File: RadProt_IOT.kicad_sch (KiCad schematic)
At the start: 10 parts, among them J1 Conn_01x04_Pin, J2 Conn_01x04_Pin, J3 Conn_01x04_Pin, J4 OUT+, J5 OUT-, J6 Conn_02x05_Top_Bottom, SW1 Config, U1 RaspberryPi_Pico_W

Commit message: gcode generated...
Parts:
- renumbered J6 to J1, J1 to UART1, J2 to UART2, J3 to UART3
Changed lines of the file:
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@@
 		(dnp no)
 		(fields_autoplaced yes)
-		(property "Reference" "J2"
-			(at 71.755 99.06 0)
+		(property "Reference" "UART2"
+			(at 71.755 101.6 0)
 			(effects
 				(font
@@
 			(project ""
 				(path "/cff4cc2a-e2ab-4a74-8ae5-5e001e0fb180"
-					(reference "J2")
+					(reference "UART2")
 					(unit 1)
 				)
@@
 		(on_board no)
 		(dnp no)
-		(property "Reference" "J3"
+		(property "Reference" "UART3"
 			(at 71.755 142.24 0)
 			(effects
@@
 			(project ""
 				(path "/cff4cc2a-e2ab-4a74-8ae5-5e001e0fb180"
-					(reference "J3")
+					(reference "UART3")
 					(unit 1)
 				)
@@
 		(dnp no)
 		(fields_autoplaced yes)
-		(property "Reference" "J1"
-			(at 71.755 55.88 0)
+		(property "Reference" "UART1"
+			(at 71.755 58.42 0)
 			(effects
 				(font
@@
 			(project ""
 				(path "/cff4cc2a-e2ab-4a74-8ae5-5e001e0fb180"
-					(reference "J1")
+					(reference "UART1")
 					(unit 1)
 				)
@@
 		(dnp no)
 		(fields_autoplaced yes)
-		(property "Reference" "J6"
+		(property "Reference" "J1"
 			(at 215.9 97.79 0)
 			(effects
@@
 			(project ""
 				(path "/cff4cc2a-e2ab-4a74-8ae5-5e001e0fb180"
-					(reference "J6")
-					(unit 1)
-				)
+					(reference "J1")
+					(unit 1)
+				)

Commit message: prepared univprepared universal board with this layout
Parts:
- removed UART1, UART2, UART3: Conn_01x04_Pin, Connector_PinHeader_2.54mm:PinHeader_1x04_P2.54mm_Vertical, symbol Connector:Conn_01x04_Pin
- added UART0, UART2, UART3: Conn_01x04_Socket, Connector_PinSocket_2.54mm:PinSocket_1x04_P2.54mm_Vertical, symbol Connector:Conn_01x04_Socket
- R1: footprint Resistor_THT:R_Axial_DIN0204_L3.6mm_D1.6mm_P5.08mm_Horizontal -> Resistor_THT:R_Axial_DIN0204_L3.6mm_D1.6mm_P7.62mm_Horizontal
- renumbered J4 to J5, J5 to J6
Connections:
- net +5V: now also UART0.1 (Pin_1), UART2.1 (Pin_1), UART3.1 (Pin_1)
- net GND: now also R1.2, UART0.4 (Pin_4), UART2.4 (Pin_4), UART3.4 (Pin_4); no longer D1.1 (K)
- net UART0_RX: now also UART0.2 (Pin_2)
- net UART2_RX: now also UART2.2 (Pin_2)
- net UART3_RX: now also UART3.2 (Pin_2)
- net at U1.12 (GPIO9): now also D1.2 (A)
- net at U1.19 (GPIO14): no longer SW1.2
- net at U1.20 (GPIO15): now also SW1.2; no longer R1.1
- new net: D1.1 (K), R1.1
- no-connect marks 24 -> 23
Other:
- moved on the sheet: D1, R1, SW1

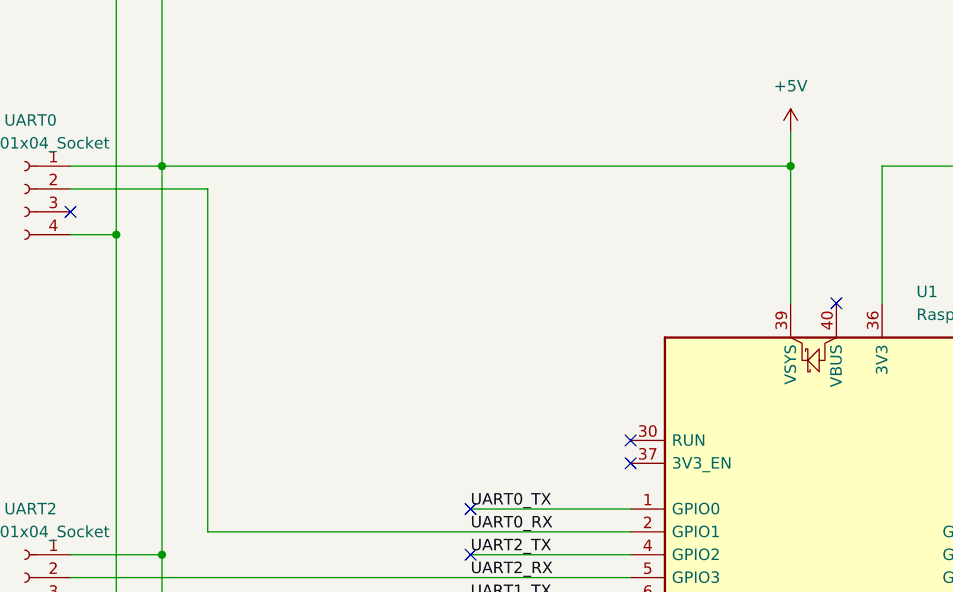
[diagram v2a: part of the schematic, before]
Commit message: added Power Ledd
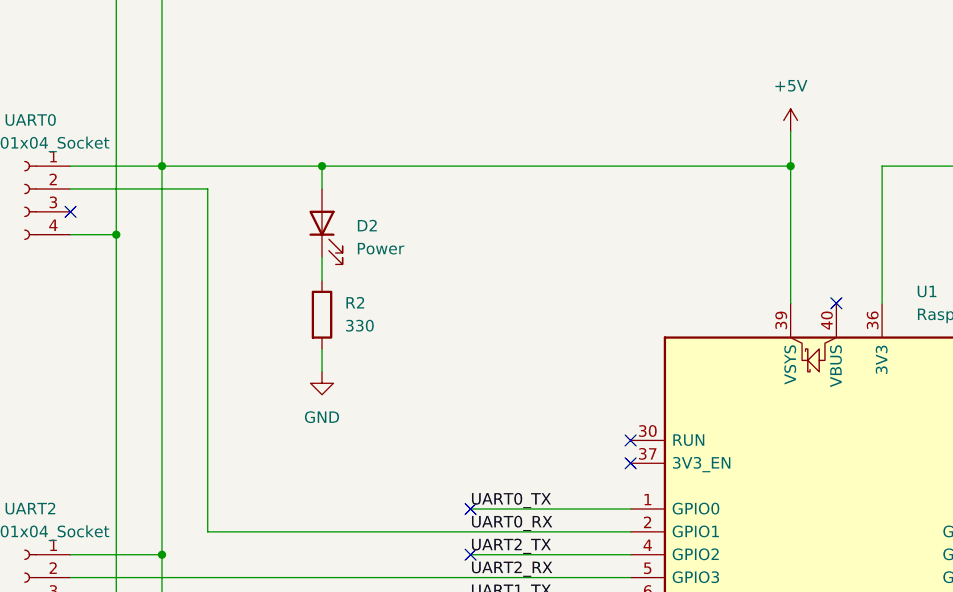
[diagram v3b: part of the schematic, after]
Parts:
- added D2: Power, LED_THT:LED_D3.0mm, symbol Device:LED
- added R2: 330, Resistor_THT:R_Axial_DIN0204_L3.6mm_D1.6mm_P7.62mm_Horizontal, symbol Device:R
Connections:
- net +5V: now also D2.2 (A)
- net GND: now also R2.2
- new net: D2.1 (K), R2.1

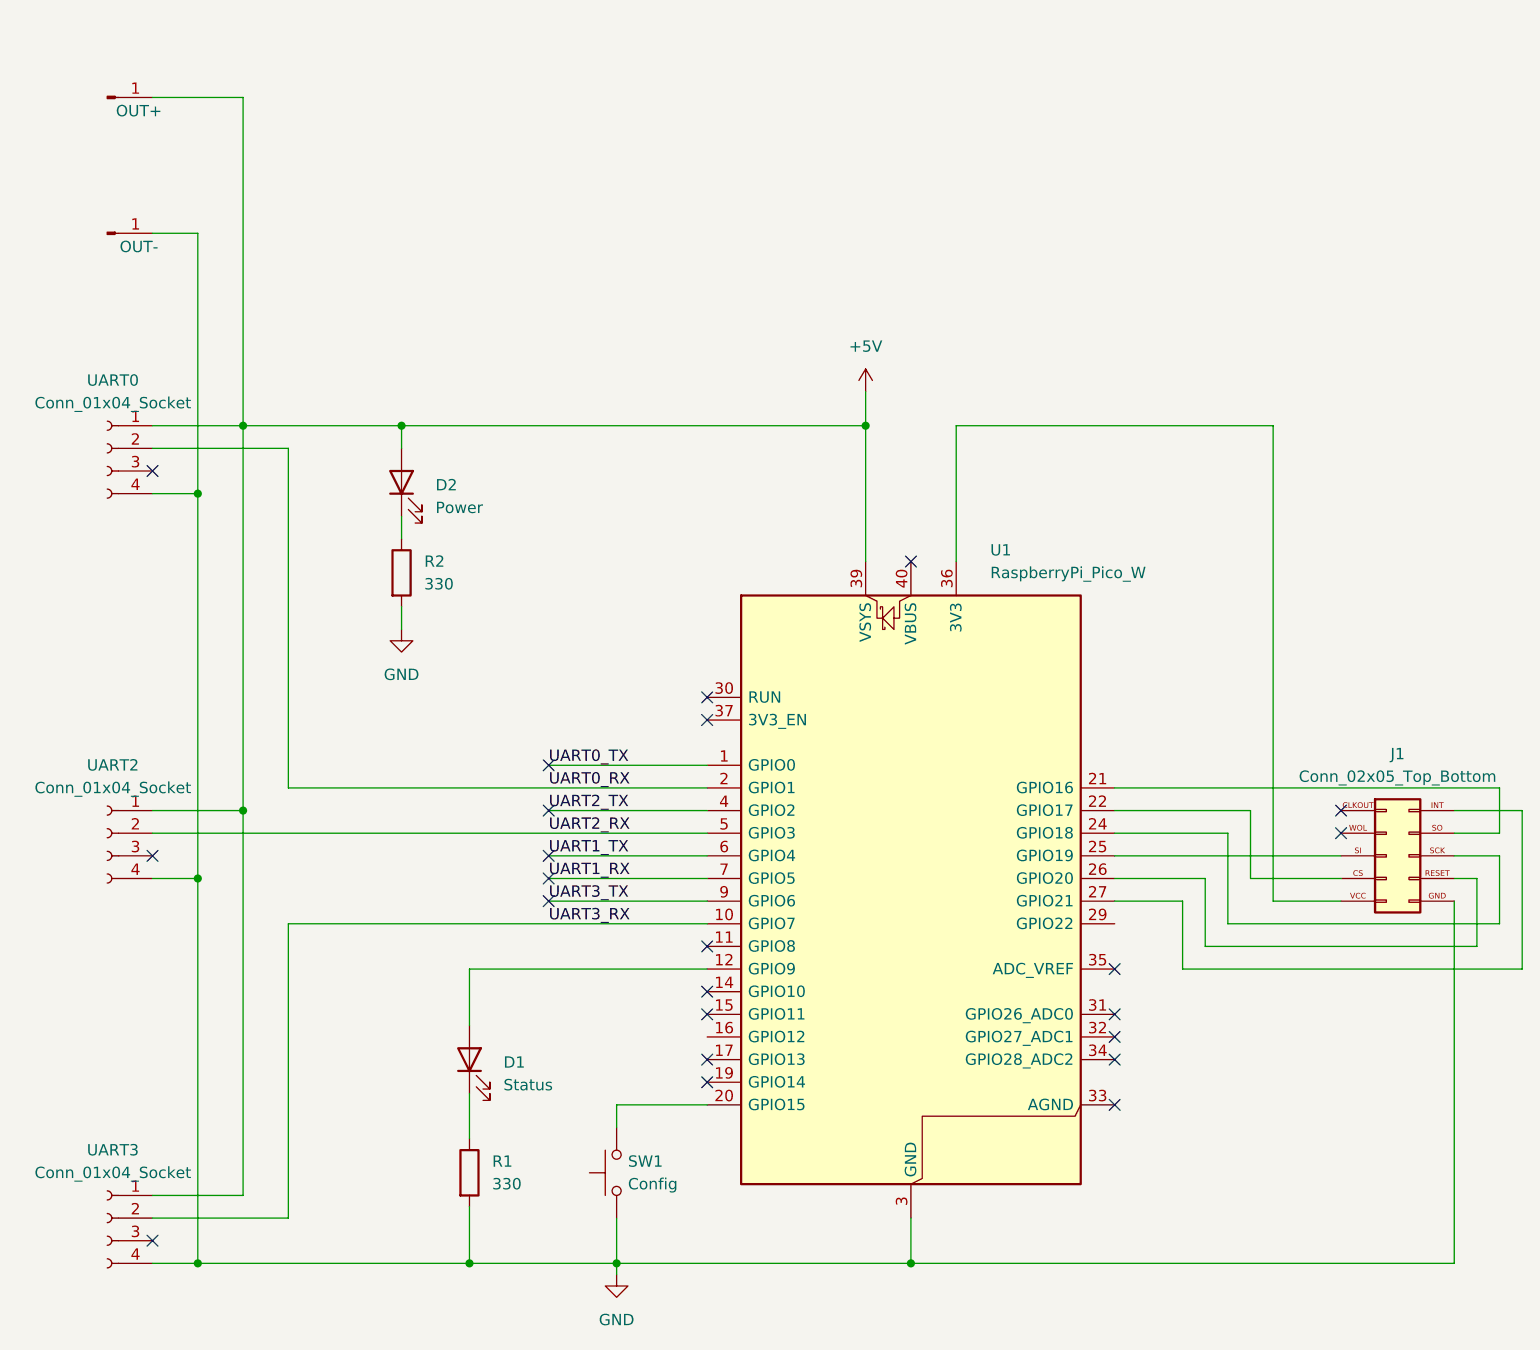
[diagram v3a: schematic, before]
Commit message: powering max3232's from 3V3 (RPi Pico's internal SMPS)
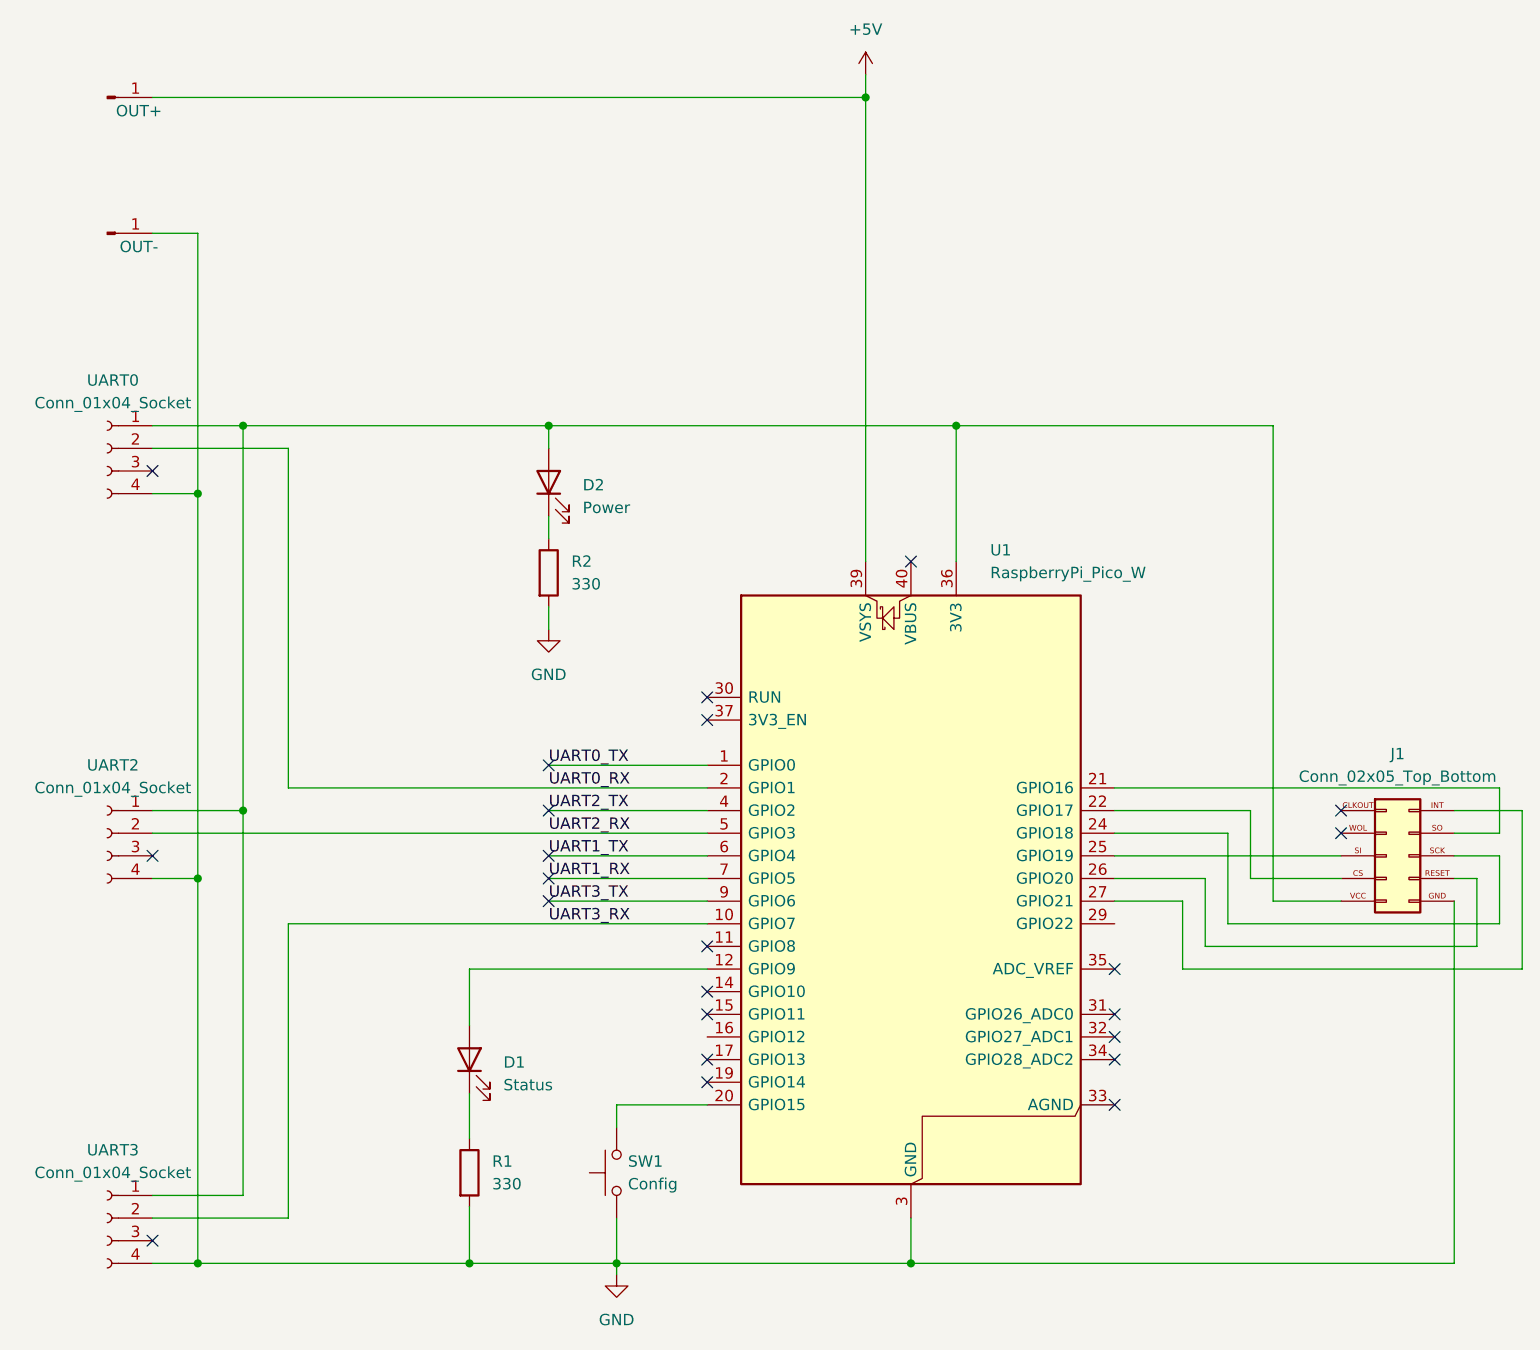
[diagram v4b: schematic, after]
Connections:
- net +5V: no longer D2.2 (A), UART0.1 (Pin_1), UART2.1 (Pin_1), UART3.1 (Pin_1)
- net at J1.VCC, U1.36 (3V3): now also D2.2 (A), UART0.1 (Pin_1), UART2.1 (Pin_1), UART3.1 (Pin_1)
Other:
- moved on the sheet: D2, R2
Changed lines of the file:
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@@
 	(paper "A4")
 	(junction
-		(at 111.76 154.94)
+		(at 166.37 60.96)
 		(diameter 0)
 		(color 0 0 0 0)
 	)
 	(junction
-		(at 156.21 60.96)
+		(at 111.76 154.94)
 		(diameter 0)
 		(color 0 0 0 0)
@@
 	)
 	(junction
-		(at 104.14 60.96)
+		(at 120.65 60.96)
 		(diameter 0)
 		(color 0 0 0 0)
 	)
 	(junction
-		(at 86.36 60.96)
+		(at 156.21 24.13)
 		(diameter 0)
 		(color 0 0 0 0)
@@
 	)
 	(junction
+		(at 86.36 60.96)
+		(diameter 0)
+		(color 0 0 0 0)
+	)
+	(junction
 		(at 81.28 154.94)
 		(diameter 0)
@@
 	(wire
 		(pts
-			(xy 104.14 60.96) (xy 104.14 63.5)
+			(xy 120.65 60.96) (xy 120.65 63.5)
 		)
 		(stroke
@@
 	(wire
 		(pts
-			(xy 104.14 71.12) (xy 104.14 73.66)
+			(xy 120.65 71.12) (xy 120.65 73.66)
 		)
 		(stroke
@@
 	(wire
 		(pts
-			(xy 156.21 60.96) (xy 156.21 76.2)
-		)
-		(stroke
-			(width 0)
-			(type default)
-		)
-	)
-	(wire
-		(pts
 			(xy 120.65 114.3) (xy 138.43 114.3)
 		)
@@
 	(wire
 		(pts
+			(xy 120.65 60.96) (xy 166.37 60.96)
+		)
+		(stroke
+			(width 0)
+			(type default)
+		)
+	)
+	(wire
+		(pts
 			(xy 184.15 104.14) (xy 199.39 104.14)
 		)
@@
 	(wire
 		(pts
+			(xy 76.2 24.13) (xy 156.21 24.13)
+		)
+		(stroke
+			(width 0)
+			(type default)
+		)
+	)
+	(wire
+		(pts
 			(xy 81.28 39.37) (xy 81.28 68.58)
 		)
@@
 	(wire
 		(pts
-			(xy 104.14 60.96) (xy 156.21 60.96)
-		)
-		(stroke
-			(width 0)
-			(type default)
-		)
-	)
-	(wire
-		(pts
 			(xy 184.15 111.76) (xy 194.31 111.76)
 		)
@@
 	(wire
 		(pts
-			(xy 104.14 81.28) (xy 104.14 83.82)
+			(xy 120.65 81.28) (xy 120.65 83.82)
 		)
 		(stroke
@@
 	(wire
 		(pts
-			(xy 76.2 24.13) (xy 86.36 24.13)
-		)
-		(stroke
-			(width 0)
-			(type default)
-		)
-	)
-	(wire
-		(pts
-			(xy 86.36 60.96) (xy 104.14 60.96)
+			(xy 201.93 60.96) (xy 166.37 60.96)
 		)
 		(stroke
@@
 	(wire
 		(pts
-			(xy 201.93 60.96) (xy 166.37 60.96)
+			(xy 76.2 106.68) (xy 138.43 106.68)
 		)
 		(stroke
@@
 	(wire
 		(pts
-			(xy 76.2 106.68) (xy 138.43 106.68)
+			(xy 128.27 154.94) (xy 161.29 154.94)
 		)
 		(stroke
@@
 	(wire
 		(pts
-			(xy 128.27 154.94) (xy 161.29 154.94)
+			(xy 156.21 24.13) (xy 156.21 76.2)
 		)
 		(stroke
@@
 	(wire
 		(pts
-			(xy 156.21 57.15) (xy 156.21 60.96)
+			(xy 194.31 111.76) (xy 194.31 119.38)
 		)
 		(stroke
@@
 	(wire
 		(pts
-			(xy 194.31 111.76) (xy 194.31 119.38)
+			(xy 76.2 104.14) (xy 86.36 104.14)
 		)
 		(stroke
@@
 	(wire
 		(pts
-			(xy 76.2 104.14) (xy 86.36 104.14)
+			(xy 156.21 24.13) (xy 156.21 21.59)
 		)
 		(stroke
@@
 	(wire
 		(pts
-			(xy 86.36 60.96) (xy 86.36 24.13)
+			(xy 86.36 60.96) (xy 120.65 60.96)
 		)
 		(stroke
@@
 	(symbol
 		(lib_id "Device:R")
-		(at 104.14 77.47 0)
+		(at 120.65 77.47 0)
 		(unit 1)
 		(exclude_from_sim no)
@@
 		(fields_autoplaced yes)
 		(property "Reference" "R2"
-			(at 106.68 76.1999 0)
+			(at 123.19 76.1999 0)
 			(effects
 				(font
@@
 		)
 		(property "Value" "330"
-			(at 106.68 78.7399 0)
+			(at 123.19 78.7399 0)
 			(effects
 				(font
@@
 		)
 		(property "Footprint" "Resistor_THT:R_Axial_DIN0204_L3.6mm_D1.6mm_P7.62mm_Horizontal"
-			(at 102.362 77.47 90)
+			(at 118.872 77.47 90)
 			(effects
 				(font
@@
 		)
 		(property "Datasheet" "~"
-			(at 104.14 77.47 0)
+			(at 120.65 77.47 0)
 			(effects
 				(font
@@
 		)
 		(property "Description" "Resistor"
-			(at 104.14 77.47 0)
+			(at 120.65 77.47 0)
 			(effects
 				(font
@@
 	(symbol
 		(lib_id "Device:LED")
-		(at 104.14 67.31 90)
+		(at 120.65 67.31 90)
 		(unit 1)
 		(exclude_from_sim no)
@@
 		(fields_autoplaced yes)
 		(property "Reference" "D2"
-			(at 107.95 67.6274 90)
+			(at 124.46 67.6274 90)
 			(effects
 				(font
@@
 		)
 		(property "Value" "Power"
-			(at 107.95 70.1674 90)
+			(at 124.46 70.1674 90)
 			(effects
 				(font
@@
 		)
 		(property "Footprint" "LED_THT:LED_D3.0mm"
-			(at 104.14 67.31 0)
+			(at 120.65 67.31 0)
 			(effects
 				(font
@@
 		)
 		(property "Datasheet" "~"
-			(at 104.14 67.31 0)
+			(at 120.65 67.31 0)
 			(effects
 				(font
@@
 		)
 		(property "Description" "Light emitting diode"
-			(at 104.14 67.31 0)
+			(at 120.65 67.31 0)
 			(effects
 				(font
@@
 		)
 		(property "Sim.Pins" "1=K 2=A"
-			(at 104.14 67.31 0)
+			(at 120.65 67.31 0)
 			(effects
 				(font
@@
 	(symbol
 		(lib_id "power:+5V")
-		(at 156.21 57.15 0)
+		(at 156.21 21.59 0)
 		(unit 1)
 		(exclude_from_sim no)
@@
 		(fields_autoplaced yes)
 		(property "Reference" "#PWR02"
-			(at 156.21 60.96 0)
+			(at 156.21 25.4 0)
 			(effects
 				(font
@@
 		)
 		(property "Value" "+5V"
-			(at 156.21 52.07 0)
+			(at 156.21 16.51 0)
 			(effects
 				(font
@@
 		)
 		(property "Footprint" ""
-			(at 156.21 57.15 0)
+			(at 156.21 21.59 0)
 			(effects
 				(font
@@
 		)
 		(property "Datasheet" ""
-			(at 156.21 57.15 0)
+			(at 156.21 21.59 0)
 			(effects
 				(font
@@
 		)
 		(property "Description" "Power symbol creates a global label with name \"+5V\""
-			(at 156.21 57.15 0)
+			(at 156.21 21.59 0)
 			(effects
 				(font
@@
 	(symbol
 		(lib_id "power:GND")
-		(at 104.14 83.82 0)
+		(at 120.65 83.82 0)
 		(unit 1)
 		(exclude_from_sim no)
@@
 		(fields_autoplaced yes)
 		(property "Reference" "#PWR03"
-			(at 104.14 90.17 0)
+			(at 120.65 90.17 0)
 			(effects
 				(font
@@
 		)
 		(property "Value" "GND"
-			(at 104.14 88.9 0)
+			(at 120.65 88.9 0)
 			(effects
 				(font
@@
 		)
 		(property "Footprint" ""
-			(at 104.14 83.82 0)
+			(at 120.65 83.82 0)
 			(effects
 				(font
@@
 		)
 		(property "Datasheet" ""
-			(at 104.14 83.82 0)
+			(at 120.65 83.82 0)
 			(effects
 				(font
@@
 		)
 		(property "Description" "Power symbol creates a global label with name \"GND\" , ground"
-			(at 104.14 83.82 0)
+			(at 120.65 83.82 0)
 			(effects
 				(font
